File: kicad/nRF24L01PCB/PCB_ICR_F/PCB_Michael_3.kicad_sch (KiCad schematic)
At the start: 2 parts, among them U1 NRF24L01_Breakout

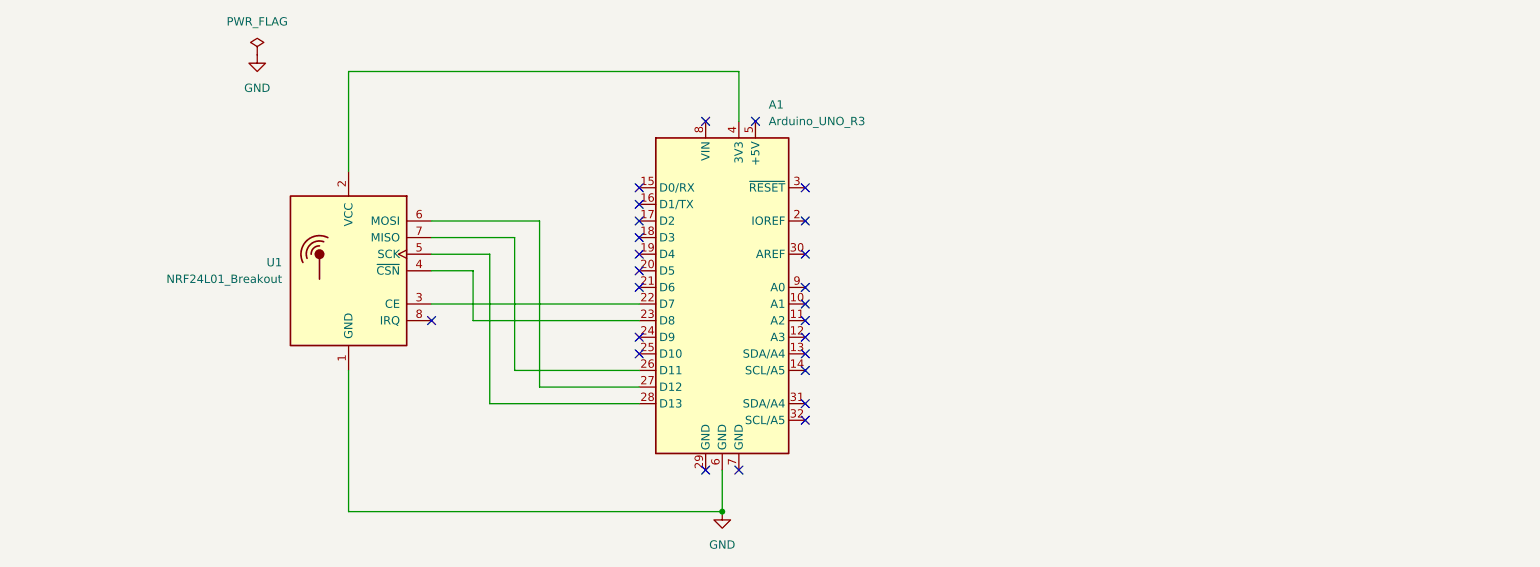
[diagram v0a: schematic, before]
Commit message: 5 servo motors now!
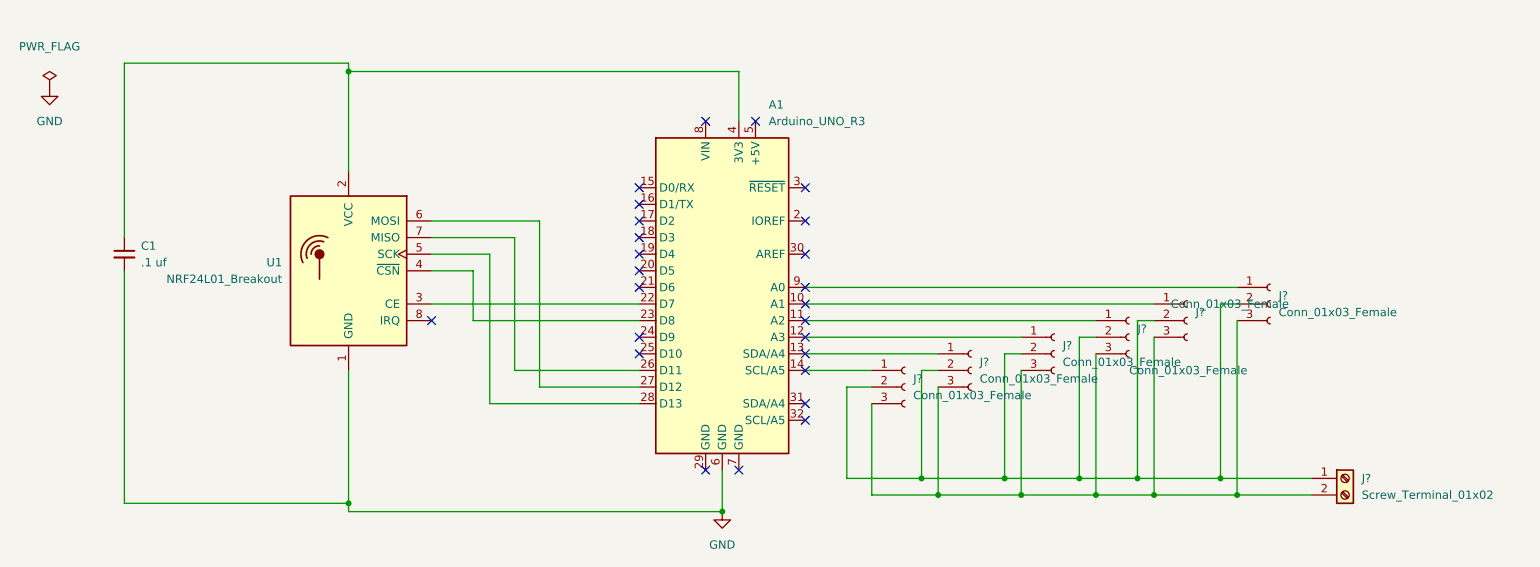
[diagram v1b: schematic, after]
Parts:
- added C1: .1 uf, Capacitor_THT:CP_Radial_Tantal_D8.0mm_P5.00mm, symbol Device:C_Small
- added J? (x6): Conn_01x03_Female, symbol Connector:Conn_01x03_Female
- added J?: Screw_Terminal_01x02, symbol Connector:Screw_Terminal_01x02
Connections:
- net GND: now also C1.2
- net at A1.4 (3V3), U1.2 (VCC): now also C1.1
- net at A1.10 (A1): now also J?.1 (Pin_1)
- net at A1.11 (A2): now also J?.1 (Pin_1)
- net at A1.12 (A3): now also J?.1 (Pin_1)
- net at A1.13 (SDA/A4): now also J?.1 (Pin_1)
- net at A1.14 (SCL/A5): now also J?.1 (Pin_1)
- net at A1.9 (A0): now also J?.1 (Pin_1)
- new net: J?.1 (Pin_1), J?.2 (Pin_2), J?.2 (Pin_2), J?.2 (Pin_2), J?.2 (Pin_2), J?.2 (Pin_2), J?.2 (Pin_2)
- new net: J?.2 (Pin_2), J?.3 (Pin_3), J?.3 (Pin_3), J?.3 (Pin_3), J?.3 (Pin_3), J?.3 (Pin_3), J?.3 (Pin_3)
